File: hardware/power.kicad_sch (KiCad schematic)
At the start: 0 parts

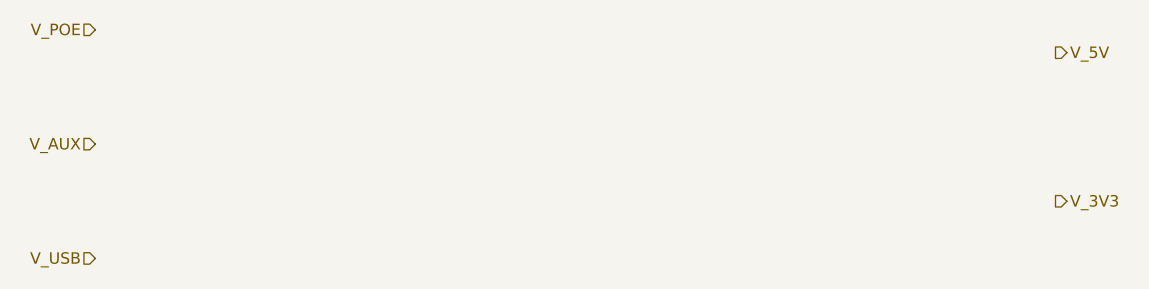
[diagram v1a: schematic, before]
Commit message: Component selection mostly done
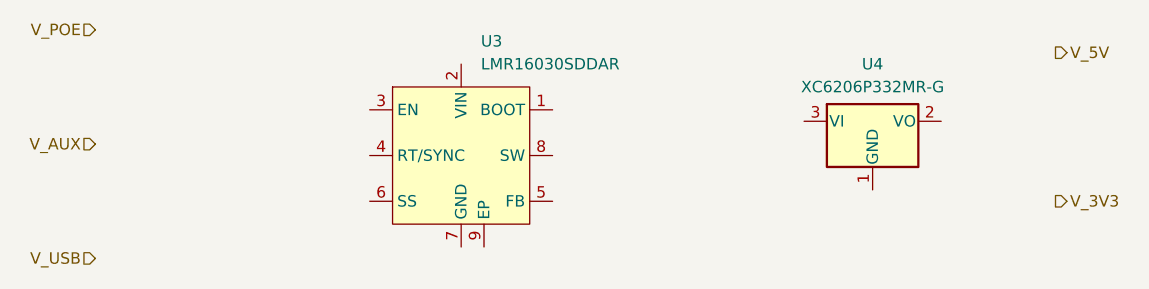
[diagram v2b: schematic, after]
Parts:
- added U3: LMR16030SDDAR, uPTP:SOIC-8_L4.9-W3.9-P1.27-LS6.0-BL-EP2.3, symbol uPTP:LMR16030SDDAR
- added U4: XC6206P332MR-G, Package_TO_SOT_SMD:SOT-23-3, symbol Regulator_Linear:XC6206PxxxMR
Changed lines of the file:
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@@
+		)
+	)
+	(symbol
+		(lib_id "uPTP:LMR16030SDDAR")
+		(at 91.44 52.07 0)
+		(unit 1)
+		(exclude_from_sim no)
+		(in_bom yes)
+		(on_board yes)
+		(dnp no)
+		(fields_autoplaced yes)
+		(property "Reference" "U3"
+			(at 93.6341 39.37 0)
+			(effects
+				(font
+					(size 1.27 1.27)
+				)
+				(justify left)
+			)
+		)
+		(property "Value" "LMR16030SDDAR"
+			(at 93.6341 41.91 0)
+			(effects
+				(font
+					(size 1.27 1.27)
+				)
+				(justify left)
+			)
+		)
+		(property "Footprint" "uPTP:SOIC-8_L4.9-W3.9-P1.27-LS6.0-BL-EP2.3"
+			(at 91.694 76.2 0)
+			(effects
+				(font
+					(size 1.27 1.27)
+				)
+				(hide yes)
+			)
+		)
+		(property "Datasheet" "https://lcsc.com/product-detail/DC-DC-Converters_TI-Tex-as-Instruments_LMR16030SDDAR_TI-Tex-as-Instruments-TI-LMR16030SDDAR_C136648.html"
+			(at 91.694 78.74 0)
+			(effects
+				(font
+					(size 1.27 1.27)
+				)
+				(hide yes)
+			)
+		)
+		(property "Description" "60V-Tolerant DC-DC Converter"
+			(at 91.186 83.82 0)
+			(effects
+				(font
+					(size 1.27 1.27)
+				)
+				(hide yes)
+			)
+		)
+		(property "LCSC Part" "C136648"
+			(at 91.694 81.28 0)
+			(effects
+				(font
+					(size 1.27 1.27)
+				)
+				(hide yes)
+			)
+		)
+		(pin "9"
+		)
+		(pin "8"
+		)
+		(pin "4"
+		)
+		(pin "1"
+		)
+		(pin "5"
+		)
+		(pin "2"
+		)
+		(pin "3"
+		)
+		(pin "7"
+		)
+		(pin "6"
+		)
+		(instances
+			(project ""
+				(path "/c29659fd-9e8d-4714-a690-4e74e6e849c2/3d1dab4d-adff-43b7-a36b-e11360ab0d63"
+					(reference "U3")
+					(unit 1)
+				)
+			)
+		)
+	)
+	(symbol
+		(lib_id "Regulator_Linear:XC6206PxxxMR")
+		(at 137.16 48.26 0)
+		(unit 1)
+		(exclude_from_sim no)
+		(in_bom yes)
+		(on_board yes)
+		(dnp no)
+		(fields_autoplaced yes)
+		(property "Reference" "U4"
+			(at 137.16 41.91 0)
+			(effects
+				(font
+					(size 1.27 1.27)
+				)
+			)
+		)
+		(property "Value" "XC6206P332MR-G"
+			(at 137.16 44.45 0)
+			(effects
+				(font
+					(size 1.27 1.27)
+				)
+			)
+		)
+		(property "Footprint" "Package_TO_SOT_SMD:SOT-23-3"
+			(at 137.16 42.545 0)
+			(effects
+				(font
+					(size 1.27 1.27)
+					(italic yes)
+				)
+				(hide yes)
+			)
+		)
+		(property "Datasheet" "https://www.torexsemi.com/file/xc6206/XC6206.pdf"
+			(at 137.16 48.26 0)
+			(effects
+				(font
+					(size 1.27 1.27)
+				)
+				(hide yes)
+			)
+		)
+		(property "Description" "Positive 60-250mA Low Dropout Regulator, Fixed Output, SOT-23"
+			(at 137.16 48.26 0)
+			(effects
+				(font
+					(size 1.27 1.27)
+				)
+				(hide yes)
+			)
+		)
+		(property "LCSC Part" "C5446"
+			(at 137.16 48.26 0)
+			(effects
+				(font
+					(size 1.27 1.27)
+				)
+				(hide yes)
+			)
+		)
+		(pin "1"
+		)
+		(pin "2"
+		)
+		(pin "3"
+		)
+		(instances
+			(project ""
+				(path "/c29659fd-9e8d-4714-a690-4e74e6e849c2/3d1dab4d-adff-43b7-a36b-e11360ab0d63"
+					(reference "U4")
+					(unit 1)
+				)
+			)
 		)
 	)

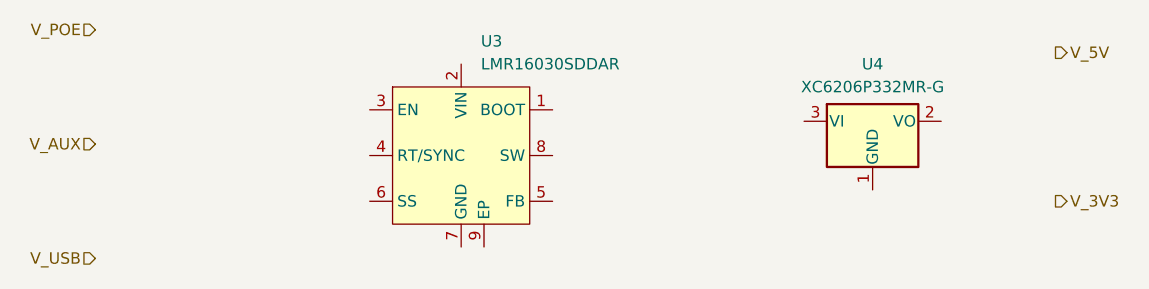
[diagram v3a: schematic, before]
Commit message: Neaten up schematic hierarchy
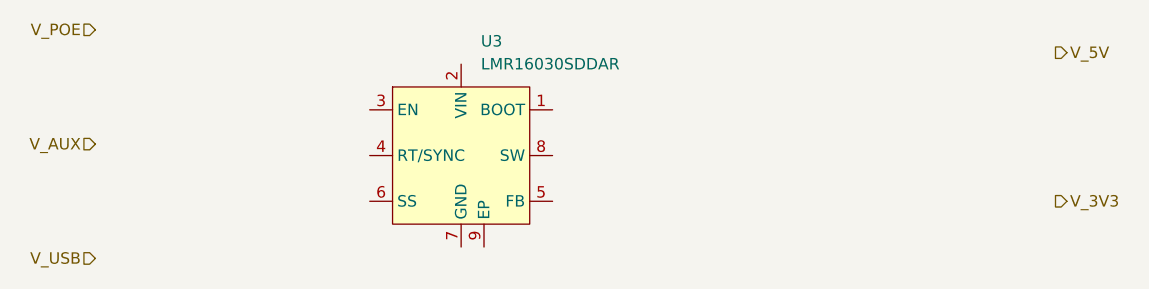
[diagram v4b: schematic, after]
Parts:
- removed U4: XC6206P332MR-G, Package_TO_SOT_SMD:SOT-23-3, symbol Regulator_Linear:XC6206PxxxMR
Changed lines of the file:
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@@
-		)
-	)
-	(symbol
-		(lib_id "Regulator_Linear:XC6206PxxxMR")
-		(at 137.16 48.26 0)
-		(unit 1)
-		(exclude_from_sim no)
-		(in_bom yes)
-		(on_board yes)
-		(dnp no)
-		(fields_autoplaced yes)
-		(property "Reference" "U4"
-			(at 137.16 41.91 0)
-			(effects
-				(font
-					(size 1.27 1.27)
-				)
-			)
-		)
-		(property "Value" "XC6206P332MR-G"
-			(at 137.16 44.45 0)
-			(effects
-				(font
-					(size 1.27 1.27)
-				)
-			)
-		)
-		(property "Footprint" "Package_TO_SOT_SMD:SOT-23-3"
-			(at 137.16 42.545 0)
-			(effects
-				(font
-					(size 1.27 1.27)
-					(italic yes)
-				)
-				(hide yes)
-			)
-		)
-		(property "Datasheet" "https://www.torexsemi.com/file/xc6206/XC6206.pdf"
-			(at 137.16 48.26 0)
-			(effects
-				(font
-					(size 1.27 1.27)
-				)
-				(hide yes)
-			)
-		)
-		(property "Description" "Positive 60-250mA Low Dropout Regulator, Fixed Output, SOT-23"
-			(at 137.16 48.26 0)
-			(effects
-				(font
-					(size 1.27 1.27)
-				)
-				(hide yes)
-			)
-		)
-		(property "LCSC Part" "C5446"
-			(at 137.16 48.26 0)
-			(effects
-				(font
-					(size 1.27 1.27)
-				)
-				(hide yes)
-			)
-		)
-		(pin "1"
-		)
-		(pin "2"
-		)
-		(pin "3"
-		)
-		(instances
-			(project ""
-				(path "/c29659fd-9e8d-4714-a690-4e74e6e849c2/3d1dab4d-adff-43b7-a36b-e11360ab0d63"
-					(reference "U4")
-					(unit 1)
-				)
-			)
 		)
 	)
